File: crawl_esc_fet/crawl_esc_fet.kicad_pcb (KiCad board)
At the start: 2 copper layers, 28 x 32 mm, 29 parts, among them Q1 (DNP)TPHR8504PL,L1Q, Q11 (DNP)TPHR8504PL,L1Q, Q3 (DNP)TPHR8504PL,L1Q, Q5 (DNP)TPHR8504PL,L1Q, Q7 (DNP)TPHR8504PL,L1Q, Q9 (DNP)TPHR8504PL,L1Q

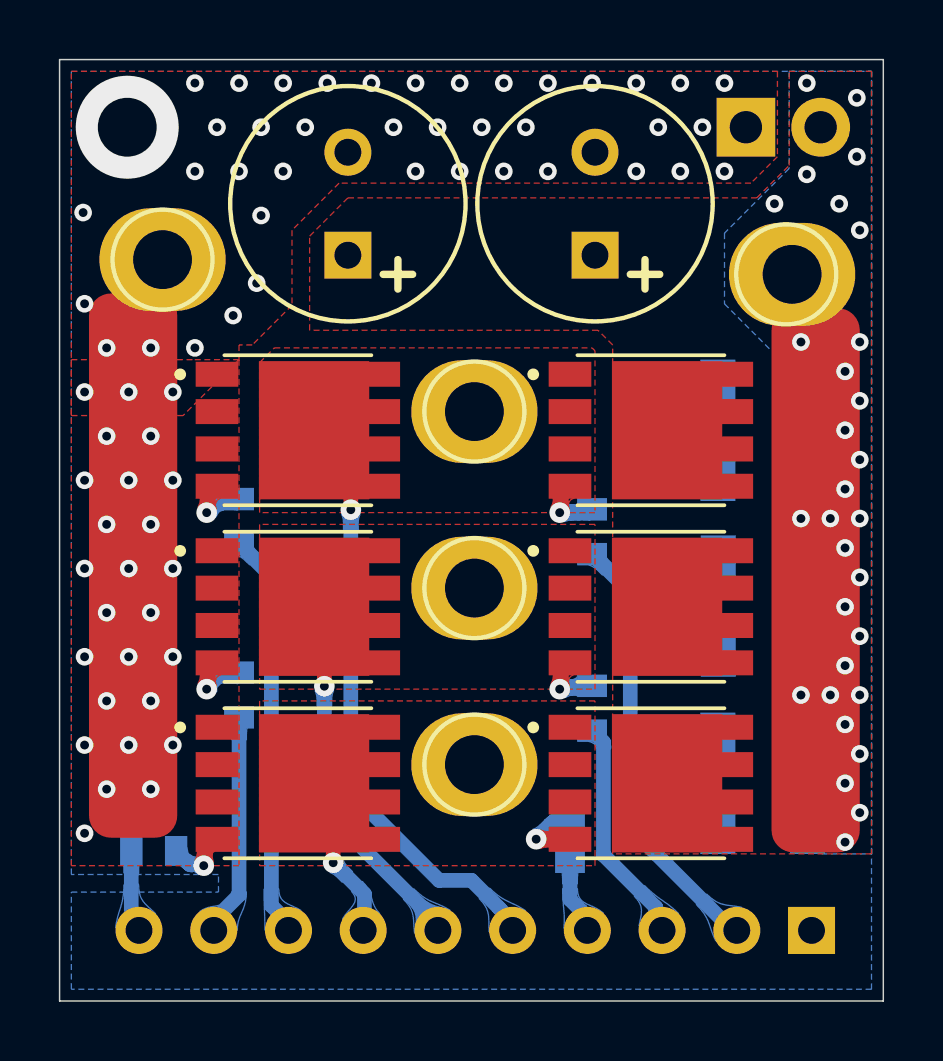
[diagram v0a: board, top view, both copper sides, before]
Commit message: change stepup isens layout
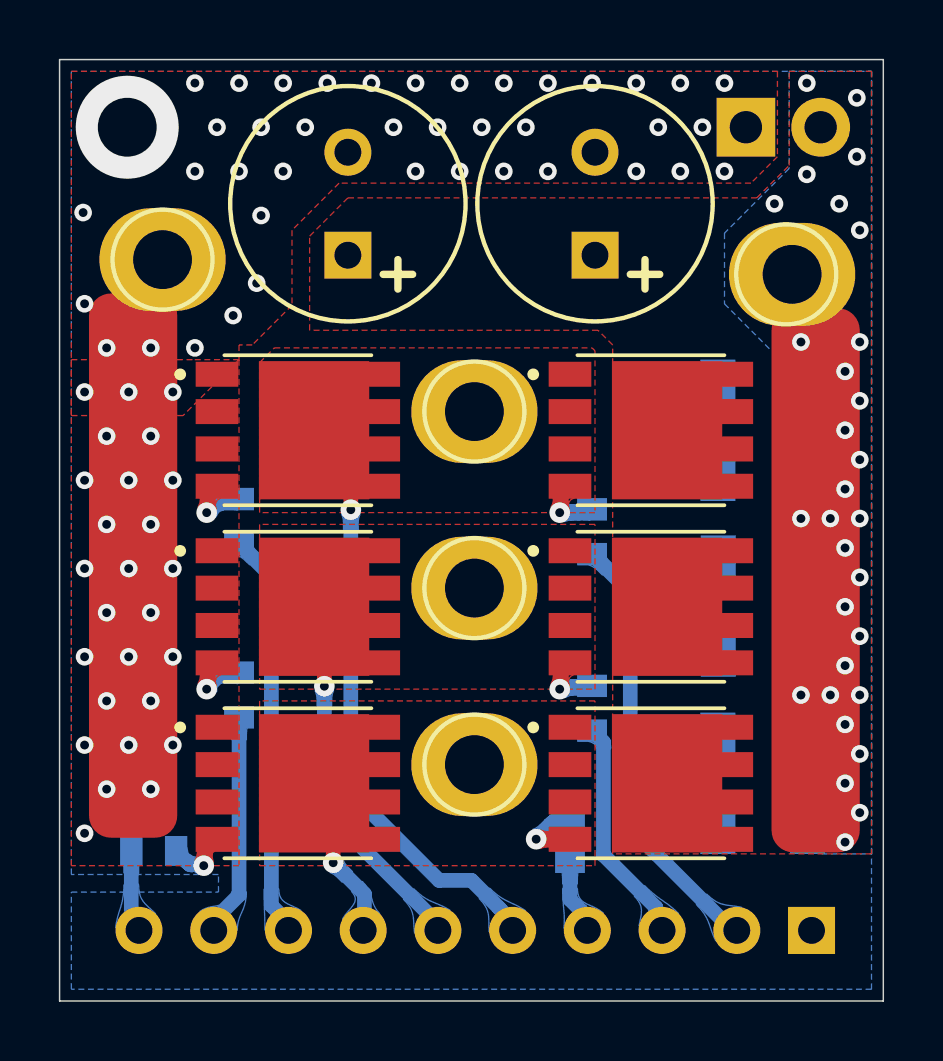
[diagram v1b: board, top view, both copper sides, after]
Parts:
- Q1, Q11, Q3, Q5, Q7, Q9: value (DNP)TPHR8504PL,L1Q -> TPHR8504PL,L1Q
